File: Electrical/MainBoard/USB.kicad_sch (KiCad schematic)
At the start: 7 parts, among them J9 USB_B_Micro, U9 MCP2221A-I_SL

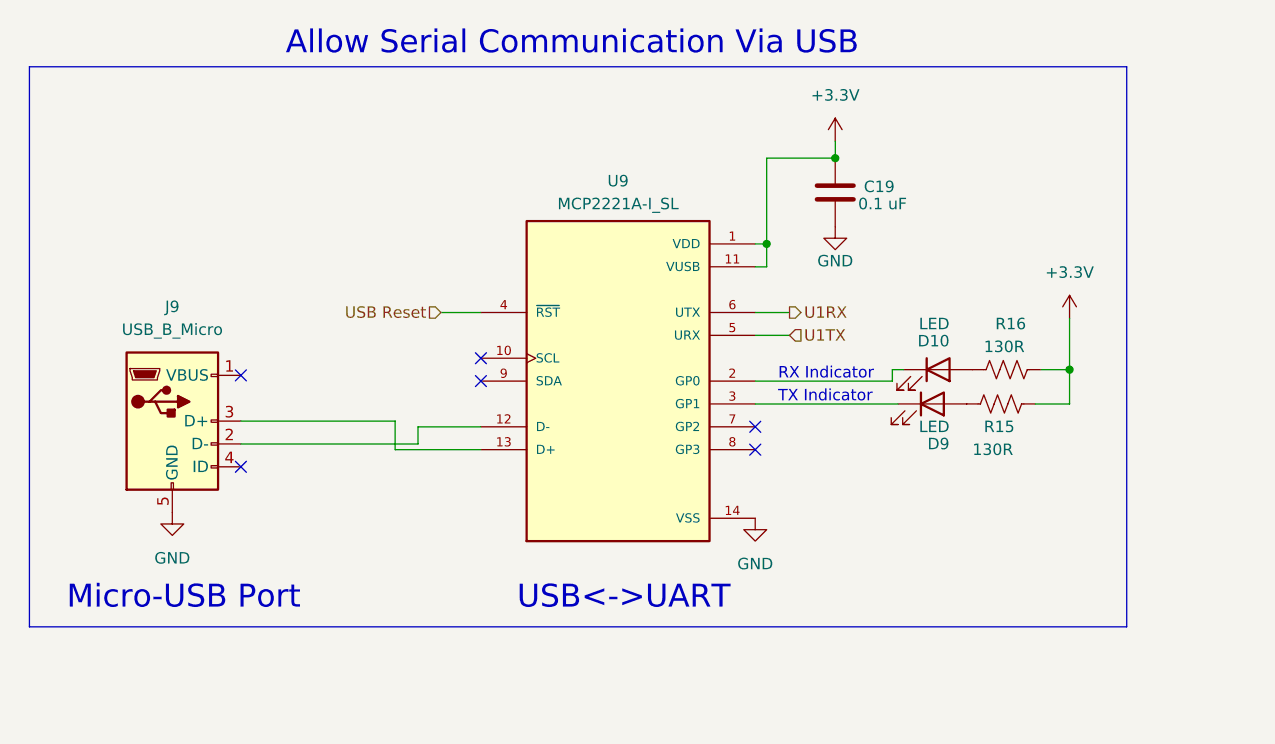
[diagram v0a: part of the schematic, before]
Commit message: Use more molex picoblades and make schematic prettier
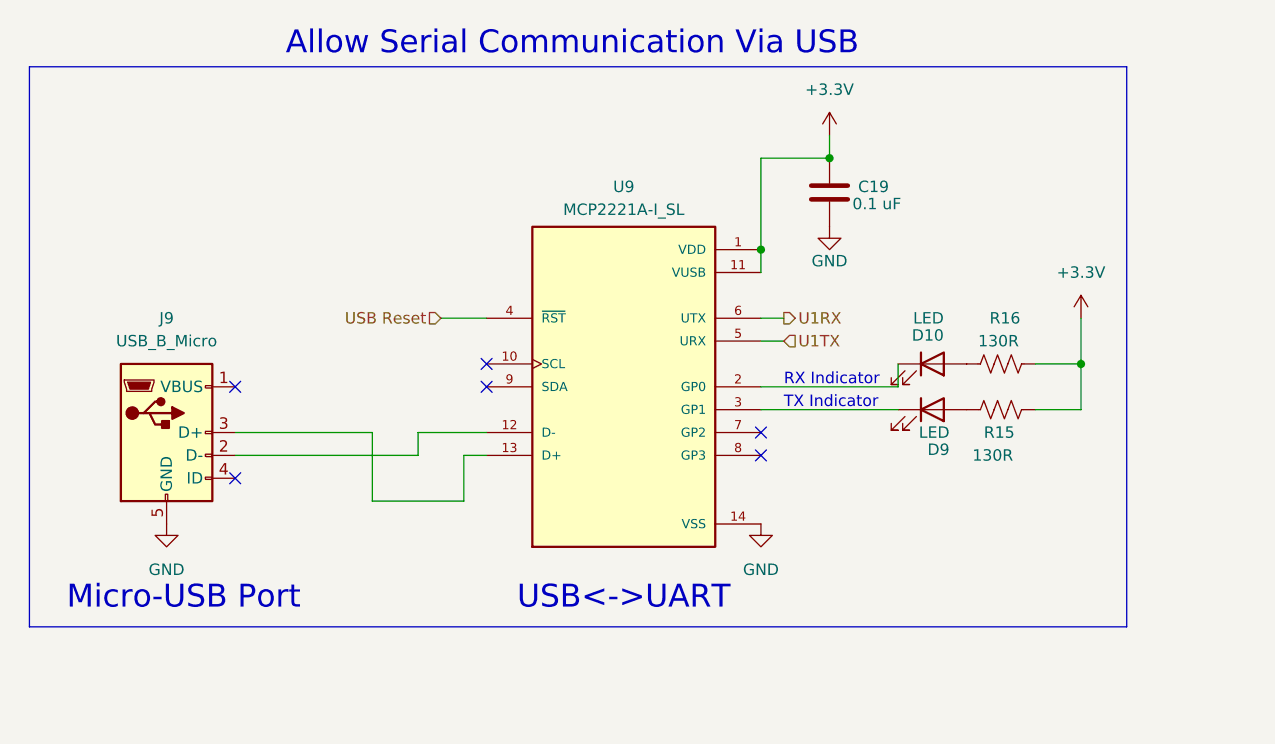
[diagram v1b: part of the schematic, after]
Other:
- moved on the sheet: C19, D10, D9, J9, R15, R16, U9
